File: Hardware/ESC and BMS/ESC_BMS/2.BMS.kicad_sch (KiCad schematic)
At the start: 38 parts, among them J301 SW IN, J302 SW OUT, Q301 SQJQ131EL, Q303 FDV304P, Q304 PMV20XNEA, Q305 SQJQ131EL, Q306 SQJQ131EL, U301 BQ2057W, U302 BQ2969

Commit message: Minor adjustments to BMS schematic - beautifying
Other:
- note added: "IF OUT=LOW (NORMAL OPERATION) -> Q303 IS ON ELSE - OVERVOLTAGE (OUT=HIGH) => Q303 IS OFF => OVP"
- note added: "IF REG=HIGH (NORMAL OPERATION) -> Q304 IS ON ELSE - UNDERVOLTAGE (REG=LOW) => Q304 IS OFF => UVP"
- note removed: "IF OUT=LOW (NORMAL OPERATION) -> Q305 IS ON ELSE - OVERVOLTAGE (OUT=HIGH) => Q305 IS OFF => OVP"
- note removed: "IF REG=HIGH (NORMAL OPERATION) -> Q305 IS ON ELSE - UNDERVOLTAGE (REG=LOW) => Q305 IS OFF => UVP"
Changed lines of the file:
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@@
 	)
 	(rectangle
-		(start 196.215 80.645)
+		(start 196.215 78.74)
 		(end 266.065 132.08)
 		(stroke
@@
 		)
 	)
-	(text "IF OUT=LOW (NORMAL OPERATION) -> Q305 IS ON\nELSE - OVERVOLTAGE (OUT=HIGH) => Q305 IS OFF => OVP"
+	(text "IF OUT=LOW (NORMAL OPERATION) -> Q303 IS ON\nELSE - OVERVOLTAGE (OUT=HIGH) => Q303 IS OFF => OVP"
 		(exclude_from_sim no)
 		(at 296.418 93.726 0)
@@
 		)
 	)
-	(text "IF REG=HIGH (NORMAL OPERATION) -> Q305 IS ON\nELSE - UNDERVOLTAGE (REG=LOW) => Q305 IS OFF => UVP"
+	(text "IF REG=HIGH (NORMAL OPERATION) -> Q304 IS ON\nELSE - UNDERVOLTAGE (REG=LOW) => Q304 IS OFF => UVP"
 		(exclude_from_sim no)
 		(at 296.672 101.092 0)
@@
 	(text "Balancing"
 		(exclude_from_sim no)
-		(at 201.676 82.55 0)
+		(at 201.422 80.518 0)
 		(effects
 			(font

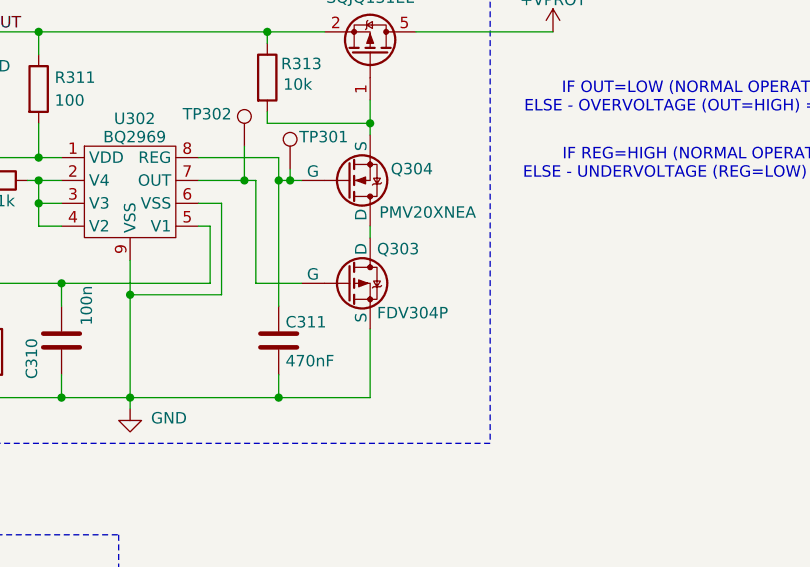
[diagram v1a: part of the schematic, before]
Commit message: fixed drain and source error bms
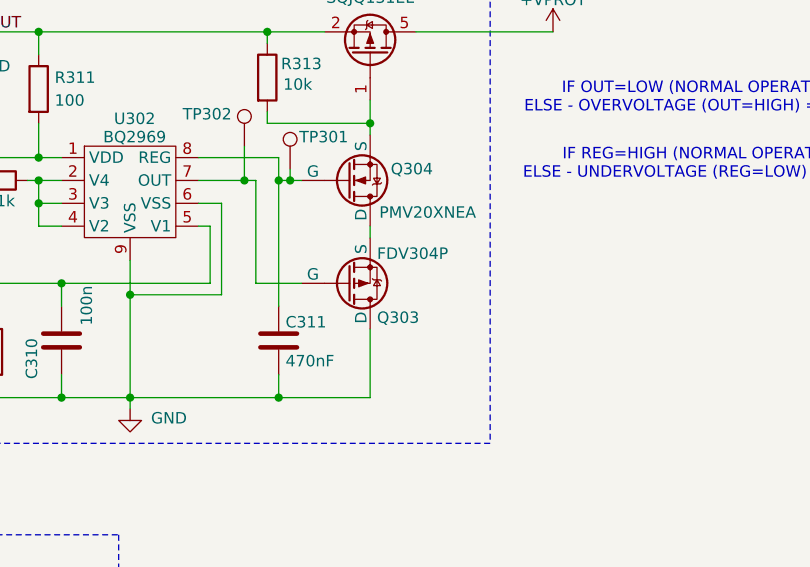
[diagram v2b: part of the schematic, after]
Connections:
- net GND: now also Q303.1 (D); no longer Q303.3 (S)
- net at Q304.1 (D): now also Q303.3 (S); no longer Q303.1 (D)
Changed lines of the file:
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@@
 		(lib_id "Simulation_SPICE:PMOS")
 		(at 250.19 114.3 0)
+		(mirror x)
 		(unit 1)
 		(exclude_from_sim no)
@@
 		(dnp no)
 		(property "Reference" "Q303"
-			(at 253.492 110.49 0)
+			(at 253.492 118.11 0)
 			(effects
 				(font
@@
 		)
 		(property "Value" "FDV304P"
-			(at 253.492 117.602 0)
+			(at 253.492 110.998 0)
 			(effects
 				(font
@@
 		)
 		(property "Footprint" "Package_TO_SOT_SMD:SOT-23"
-			(at 255.27 111.76 0)
+			(at 255.27 116.84 0)
 			(effects
 				(font
@@
 		)
 		(property "Datasheet" "https://docs.rs-online.com/d95a/0900766b800ae907.pdf"
-			(at 250.19 127 0)
+			(at 250.19 101.6 0)
 			(effects
 				(font
@@
 		)
 		(property "Sim.Device" "PMOS"
-			(at 250.19 131.445 0)
+			(at 250.19 97.155 0)
 			(effects
 				(font
@@
 		)
 		(property "Sim.Type" "VDMOS"
-			(at 250.19 133.35 0)
+			(at 250.19 95.25 0)
 			(effects
 				(font
@@
 		)
 		(property "Sim.Pins" "1=D 2=G 3=S"
-			(at 250.19 129.54 0)
+			(at 250.19 99.06 0)
 			(effects
 				(font
